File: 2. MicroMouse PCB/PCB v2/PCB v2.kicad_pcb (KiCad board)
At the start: 2 copper layers, 65 x 85 mm, 85 parts, among them Q1 S8550, SW0 SW_Push, SW1 SW_Push, SW2 SW_Push, SW3 SW_Push, SW4 SW_Push, U1 STM32F407VGTx, U2 LM2596S-5, U3 AMS1117-3.3, U4 TB6612FNG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

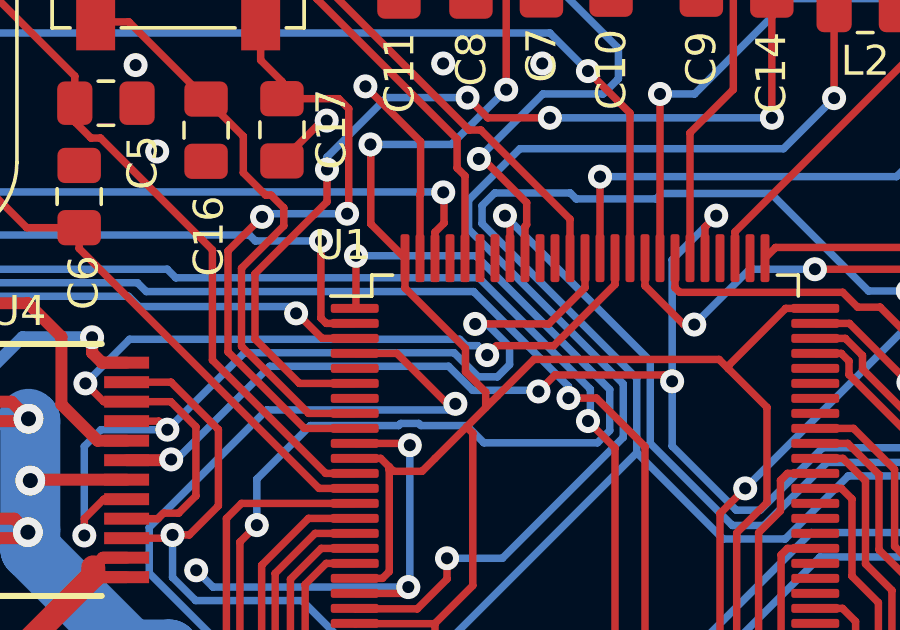
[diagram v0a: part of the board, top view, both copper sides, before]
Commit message: added PID for turning and solved hardfault
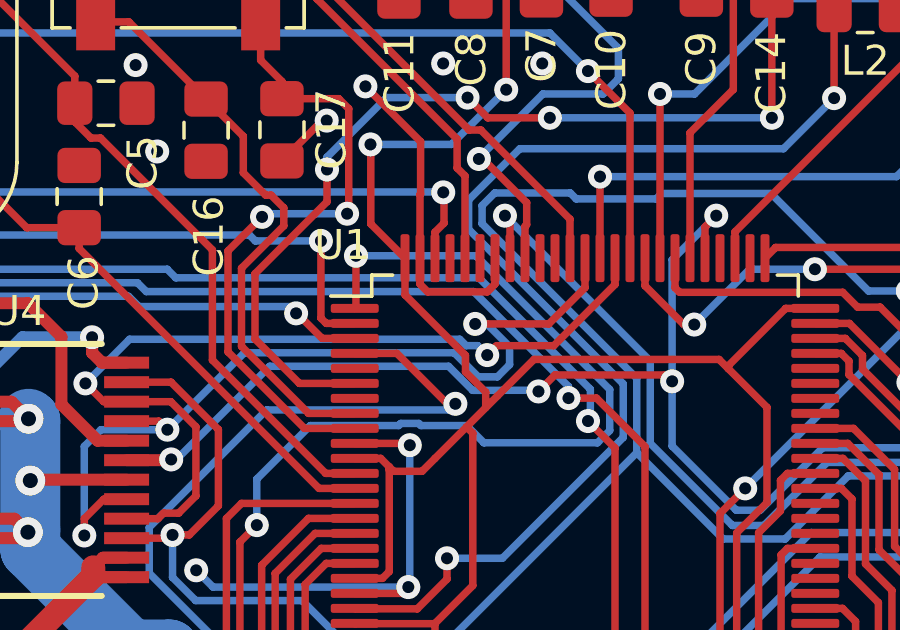
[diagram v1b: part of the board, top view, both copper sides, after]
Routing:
- net GND: track 176.8 -> 181.3 mm
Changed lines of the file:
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@@
   (segment (start 124.8 80.87) (end 125.37 81.44) (width 0.4) (layer "F.Cu") (net 1))
   (segment (start 163.65 85.33) (end 166.01 85.33) (width 0.4) (layer "F.Cu") (net 1))
+  (segment (start 138.42 76.950686) (end 138.42 76.085) (width 0.25) (layer "F.Cu") (net 1))
   (segment (start 154.7 80.226522) (end 152.733478 78.26) (width 0.25) (layer "F.Cu") (net 1))
   (segment (start 125.43 83.5) (end 125.46 83.47) (width 0.4) (layer "F.Cu") (net 1))
@@
   (segment (start 165.163344 88.4304) (end 166.0604 88.4304) (width 2) (layer "F.Cu") (net 1))
   (segment (start 169.9625 108.2925) (end 170.93 108.2925) (width 2) (layer "F.Cu") (net 1))
+  (segment (start 140.92 76.950686) (end 140.660686 77.21) (width 0.25) (layer "F.Cu") (net 1))
   (segment (start 121.39 81.52) (end 125.29 81.52) (width 0.4) (layer "F.Cu") (net 1))
   (segment (start 163.48 85.5) (end 163.46 85.52) (width 2) (layer "F.Cu") (net 1))
@@
   (segment (start 121.39 85.42) (end 125.15 85.42) (width 0.4) (layer "F.Cu") (net 1))
   (segment (start 137.82 87.26) (end 136.245 87.26) (width 0.25) (layer "F.Cu") (net 1))
+  (segment (start 138.679314 77.21) (end 138.42 76.950686) (width 0.25) (layer "F.Cu") (net 1))
+  (segment (start 140.92 76.085) (end 140.92 76.950686) (width 0.25) (layer "F.Cu") (net 1))
   (segment (start 138.42 92.72) (end 137.2075 93.9325) (width 0.25) (layer "F.Cu") (net 1))
+  (segment (start 140.660686 77.21) (end 138.679314 77.21) (width 0.25) (layer "F.Cu") (net 1))
   (segment (start 163.48 81.97) (end 164.02 81.43) (width 0.4) (layer "F.Cu") (net 1))
   (segment (start 124.9 84.77) (end 125.35 85.22) (width 0.4) (layer "F.Cu") (net 1))
@@
   (segment (start 118.0735 125.41) (end 118.0735 134.9615) (width 0.25) (layer "F.Cu") (net 3))
   (segment (start 137.110686 82.76) (end 136.245 82.76) (width 0.25) (layer "F.Cu") (net 3))
-  (segment (start 137.92 77.08) (end 137.92 76.085) (width 0.25) (layer "F.Cu") (net 3))
   (segment (start 160.2522 131.3354) (end 161.8876 129.7) (width 0.25) (layer "F.Cu") (net 3))
   (segment (start 148.7009 79.7729) (end 148.7009 79.6691) (width 0.25) (layer "F.Cu") (net 3))
@@
   (segment (start 133.0647 124.1838) (end 141.3363 124.1838) (width 0.25) (layer "F.Cu") (net 3))
   (segment (start 138.91 88.27) (end 136.255 88.27) (width 0.25) (layer "F.Cu") (net 3))
-  (segment (start 139.936 79.876) (end 139.936 79.096) (width 0.25) (layer "F.Cu") (net 3))
   (segment (start 143.33 122.3801) (end 143.33 120.129905) (width 0.25) (layer "F.Cu") (net 3))
   (segment (start 140.9994 80.6806) (end 138.92 82.76) (width 0.25) (layer "F.Cu") (net 3))
+  (segment (start 137.92 77.31) (end 137.92 76.085) (width 0.25) (layer "F.Cu") (net 3))
   (segment (start 144.7885 65.38) (end 147.7985 65.38) (width 0.25) (layer "F.Cu") (net 3))
   (segment (start 144.01 113.688174) (end 144.01 104.64) (width 0.25) (layer "F.Cu") (net 3))
@@
   (segment (start 149.92 90.4663) (end 148.9763 89.5226) (width 0.25) (layer "F.Cu") (net 3))
   (segment (start 131.8385 125.41) (end 133.0647 124.1838) (width 0.25) (layer "F.Cu") (net 3))
+  (segment (start 139.936 79.876) (end 139.936 79.326) (width 0.25) (layer "F.Cu") (net 3))
   (segment (start 120.216 125.38) (end 118.1035 125.38) (width 0.25) (layer "F.Cu") (net 3))
   (segment (start 129.7785 125.46) (end 128.6964 126.5421) (width 0.25) (layer "F.Cu") (net 3))
-  (segment (start 139.936 79.096) (end 137.92 77.08) (width 0.25) (layer "F.Cu") (net 3))
   (segment (start 165.4353 126.4432) (end 161.8876 126.4432) (width 0.25) (layer "F.Cu") (net 3))
   (segment (start 161.8876 129.7) (end 161.8876 126.4432) (width 0.25) (layer "F.Cu") (net 3))
@@
   (segment (start 136.255 88.27) (end 136.245 88.26) (width 0.25) (layer "F.Cu") (net 3))
   (segment (start 148.7009 79.6691) (end 150.61 77.76) (width 0.25) (layer "F.Cu") (net 3))
-  (segment (start 140.61 80.55) (end 139.936 79.876) (width 0.25) (layer "F.Cu") (net 3))
   (segment (start 148.0039 57.3989) (end 147.3261 58.0767) (width 0.25) (layer "F.Cu") (net 3))
   (segment (start 137.540686 83.19) (end 137.3947 83.044014) (width 0.25) (layer "F.Cu") (net 3))
@@
   (segment (start 128.6964 126.5421) (end 125.2369 126.5421) (width 0.25) (layer "F.Cu") (net 3))
   (segment (start 131.8385 125.46) (end 131.8385 126.8763) (width 0.25) (layer "F.Cu") (net 3))
+  (segment (start 140.61 80.55) (end 139.936 79.876) (width 0.25) (layer "F.Cu") (net 3))
+  (segment (start 140.61 81.07) (end 140.61 80.55) (width 0.25) (layer "F.Cu") (net 3))
   (segment (start 156.4785 65.29) (end 154.3085 65.29) (width 0.25) (layer "F.Cu") (net 3))
   (segment (start 141.3363 124.1838) (end 142.4345 125.282) (width 0.25) (layer "F.Cu") (net 3))
   (segment (start 123.0089 124.3141) (end 121.2819 124.3141) (width 0.25) (layer "F.Cu") (net 3))
   (segment (start 142.2186 79.4614) (end 140.9994 80.6806) (width 0.25) (layer "F.Cu") (net 3))
-  (segment (start 140.61 81.07) (end 140.61 80.55) (width 0.25) (layer "F.Cu") (net 3))
   (segment (start 131.8385 125.46) (end 131.8385 125.41) (width 0.25) (layer "F.Cu") (net 3))
   (segment (start 143.74 113.958174) (end 144.01 113.688174) (width 0.25) (layer "F.Cu") (net 3))
@@
   (segment (start 142.4685 125.316) (end 144.5585 125.316) (width 0.25) (layer "F.Cu") (net 3))
   (segment (start 161.8876 126.4432) (end 159.702 124.2576) (width 0.25) (layer "F.Cu") (net 3))
+  (segment (start 139.936 79.326) (end 137.92 77.31) (width 0.25) (layer "F.Cu") (net 3))
   (segment (start 149.9851 81.0571) (end 148.7009 79.7729) (width 0.25) (layer "F.Cu") (net 3))
   (segment (start 131.8385 125.46) (end 129.7785 125.46) (width 0.25) (layer "F.Cu") (net 3))
